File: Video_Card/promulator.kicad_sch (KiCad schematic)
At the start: 16 parts, among them J2 Conn_01x06_Pin, J3 Conn_01x05_Socket, U5 PIC18F15Q40, U7 EPF81188AQC208-3

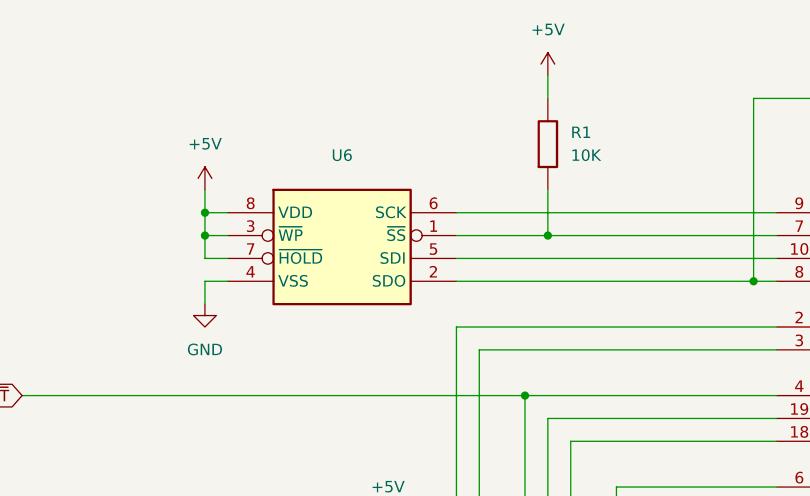
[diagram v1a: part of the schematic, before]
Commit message: Todays work:
* Added clock identifier to SPI flash clock input
* Add config pins to FPGA host interface - can be used for configuring address decoding
* Add FPGA clocks sheet
* Add expansion ROM sheet
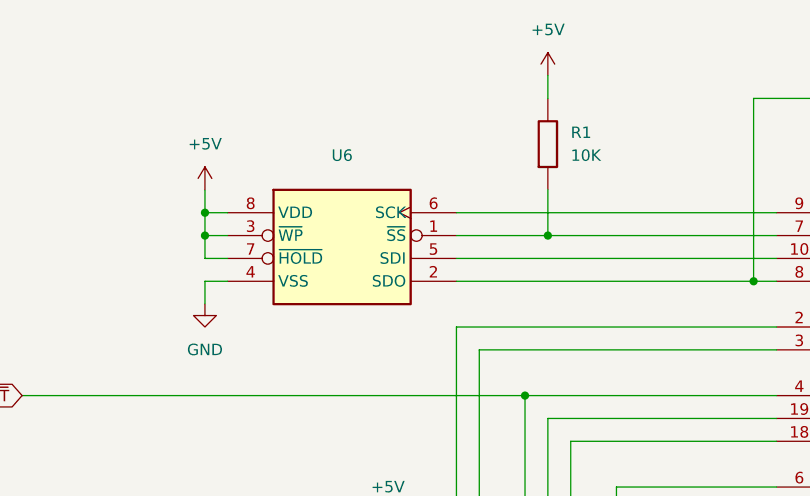
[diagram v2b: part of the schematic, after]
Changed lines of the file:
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@@
 	)
 	(symbol
-		(lib_name "Video_Card:FPGA_dev")
 		(lib_id "Video_Card:FPGA_dev")
 		(at 48.26 175.26 0)
@@
 		)
 		(pin "154"
+		)
+		(pin ""
+		)
+		(pin ""
+		)
+		(pin ""
+		)
+		(pin ""
+		)
+		(pin ""
+		)
+		(pin ""
+		)
+		(pin ""
+		)
+		(pin ""
+		)
+		(pin ""
+		)
+		(pin ""
+		)
+		(pin ""
+		)
+		(pin ""
+		)
+		(pin ""
+		)
+		(pin ""
+		)
+		(pin ""
+		)
+		(pin ""
 		)
 		(pin ""
@@
 	)
 	(symbol
+		(lib_name "Video_Card:FPGA_dev")
 		(lib_id "Video_Card:FPGA_dev")
 		(at 215.9 50.8 0)
@@
 		)
 		(pin ""
+		)
+		(pin ""
+		)
+		(pin ""
+		)
+		(pin ""
+		)
+		(pin ""
+		)
+		(pin ""
+		)
+		(pin ""
+		)
+		(pin ""
+		)
+		(pin ""
+		)
+		(pin ""
+		)
+		(pin ""
+		)
+		(pin ""
+		)
+		(pin ""
+		)
+		(pin ""
+		)
+		(pin ""
+		)
+		(pin ""
+		)
+		(pin ""

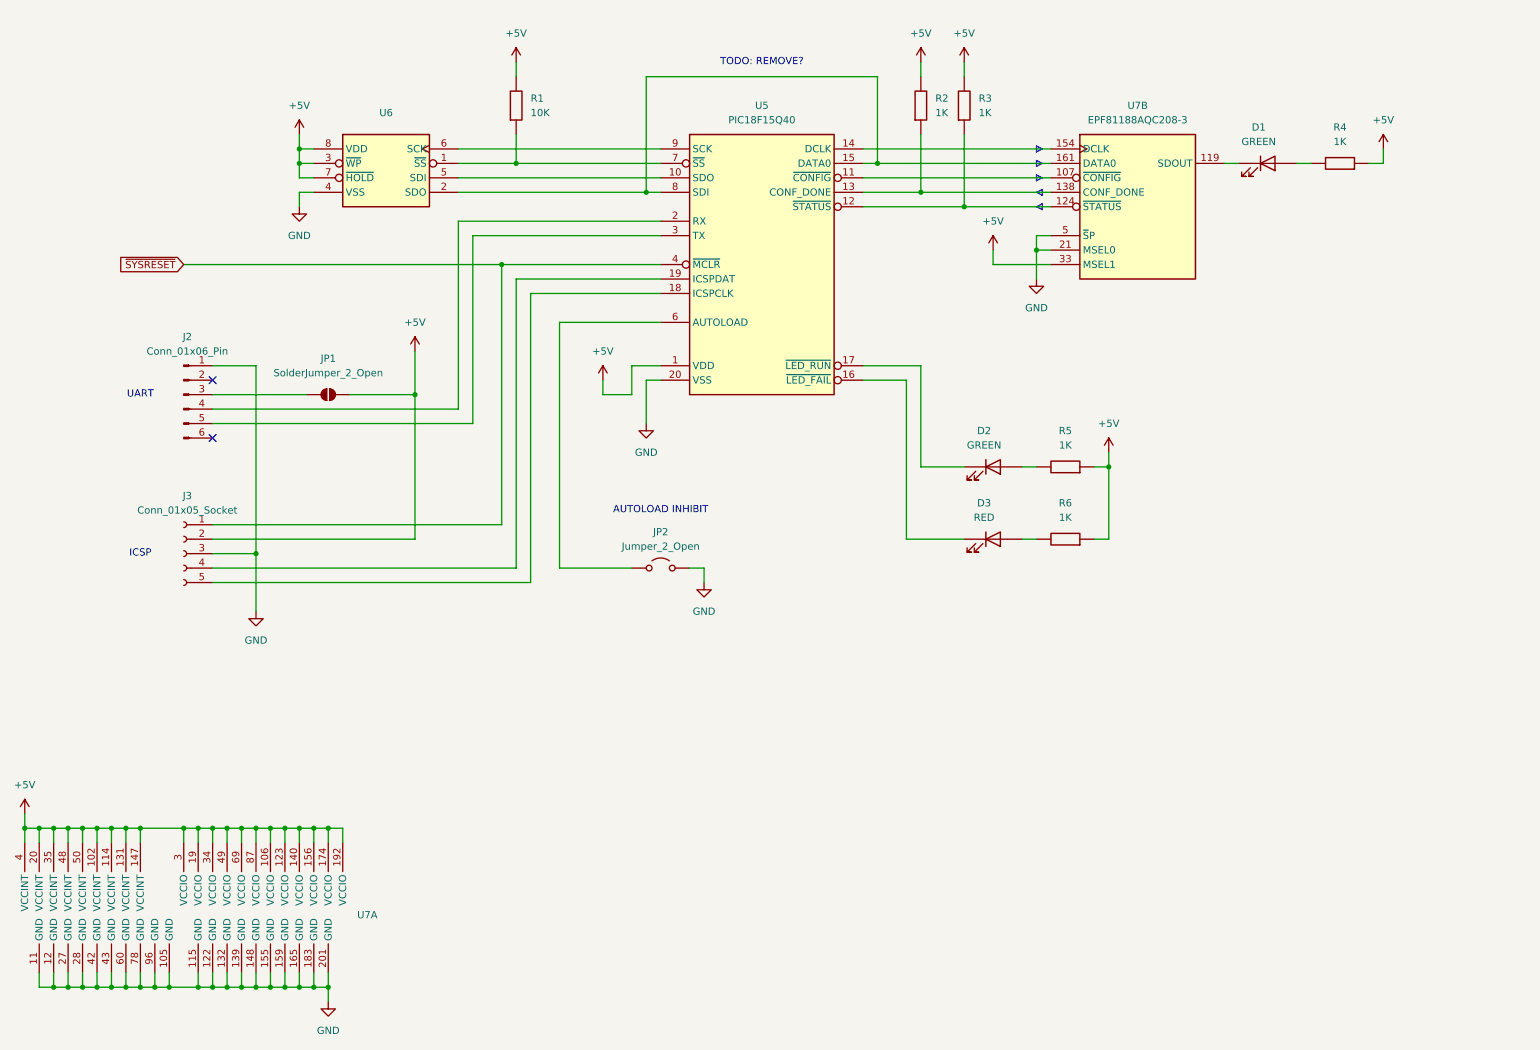
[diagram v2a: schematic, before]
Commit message: Work to date:
* added RAMDAC sheet
* tweaks to promulator circuit to disconnect MCLR, and add future reset output
* tweaks to FPGA host interface, add pin numbers and rearrange reset input to allow reset either from the system or from the promulator following configuration
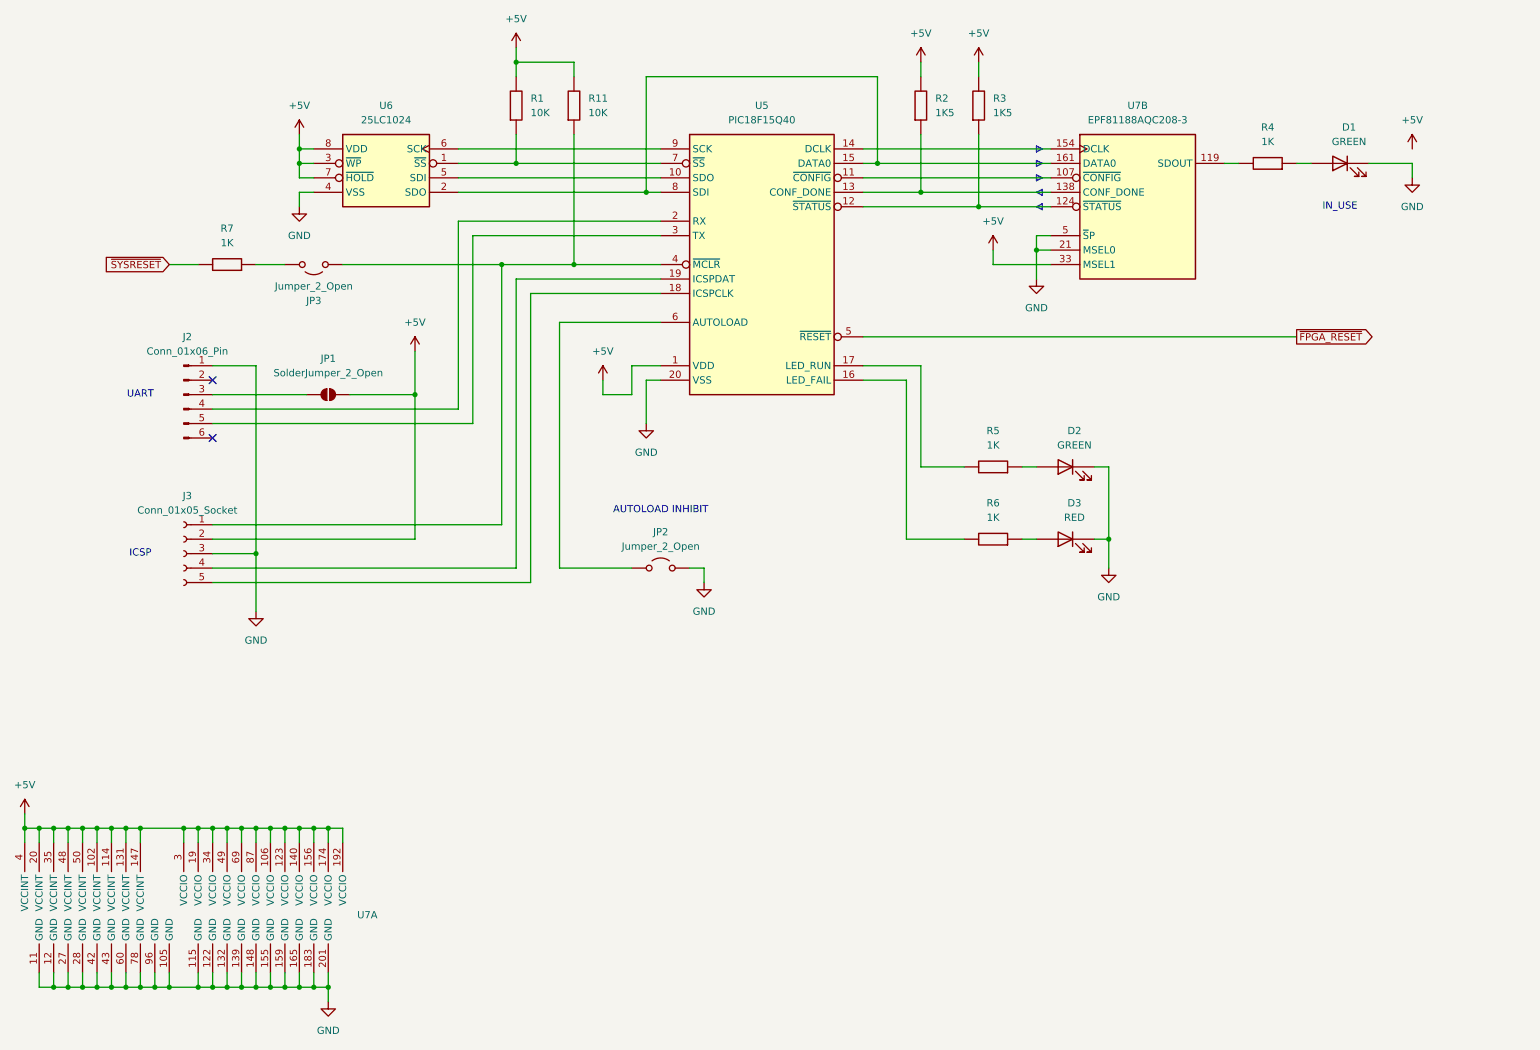
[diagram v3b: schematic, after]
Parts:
- added JP3: Jumper_2_Open, Connector_PinHeader_2.54mm:PinHeader_1x02_P2.54mm_Vertical, symbol Jumper:Jumper_2_Open
- added R11: 10K, COMET_footprints:R_SMD0805, symbol COMET_symbols:R
- added R7: 1K, COMET_footprints:R_SMD0805, symbol COMET_symbols:R
- R2, R3: value 1K -> 1K5
- U6: value ~ -> 25LC1024
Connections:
- net +5V: now also R11.1; no longer R4.2, R5.2, R6.2
- net GND: now also D1.1 (K), D2.1 (K), D3.1 (K)
- net ~{SYSRESET}: now also R7.1; no longer J3.1 (Pin_1), U5.4 (~{MCLR})
- net at R5.1: now also U5.17 (LED_RUN); no longer D2.2 (A)
- net at R6.1: now also U5.16 (LED_FAIL); no longer D3.2 (A)
- net at U7.119 (SDOUT): now also R4.1; no longer D1.1 (K)
- net at D1.2 (A): now also R4.2; no longer R4.1
- new net: J3.1 (Pin_1), JP3.2 (B), R11.2, U5.4 (~{MCLR})
- new net: D2.2 (A), R5.2
- new net: JP3.1 (A), R7.2
- new net: D3.2 (A), R6.2
- new net ~{FPGA_RESET}: U5.5 (~{RESET})
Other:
- note added: "IN_USE"
- note removed: "TODO: REMOVE?"
- moved on the sheet: R3

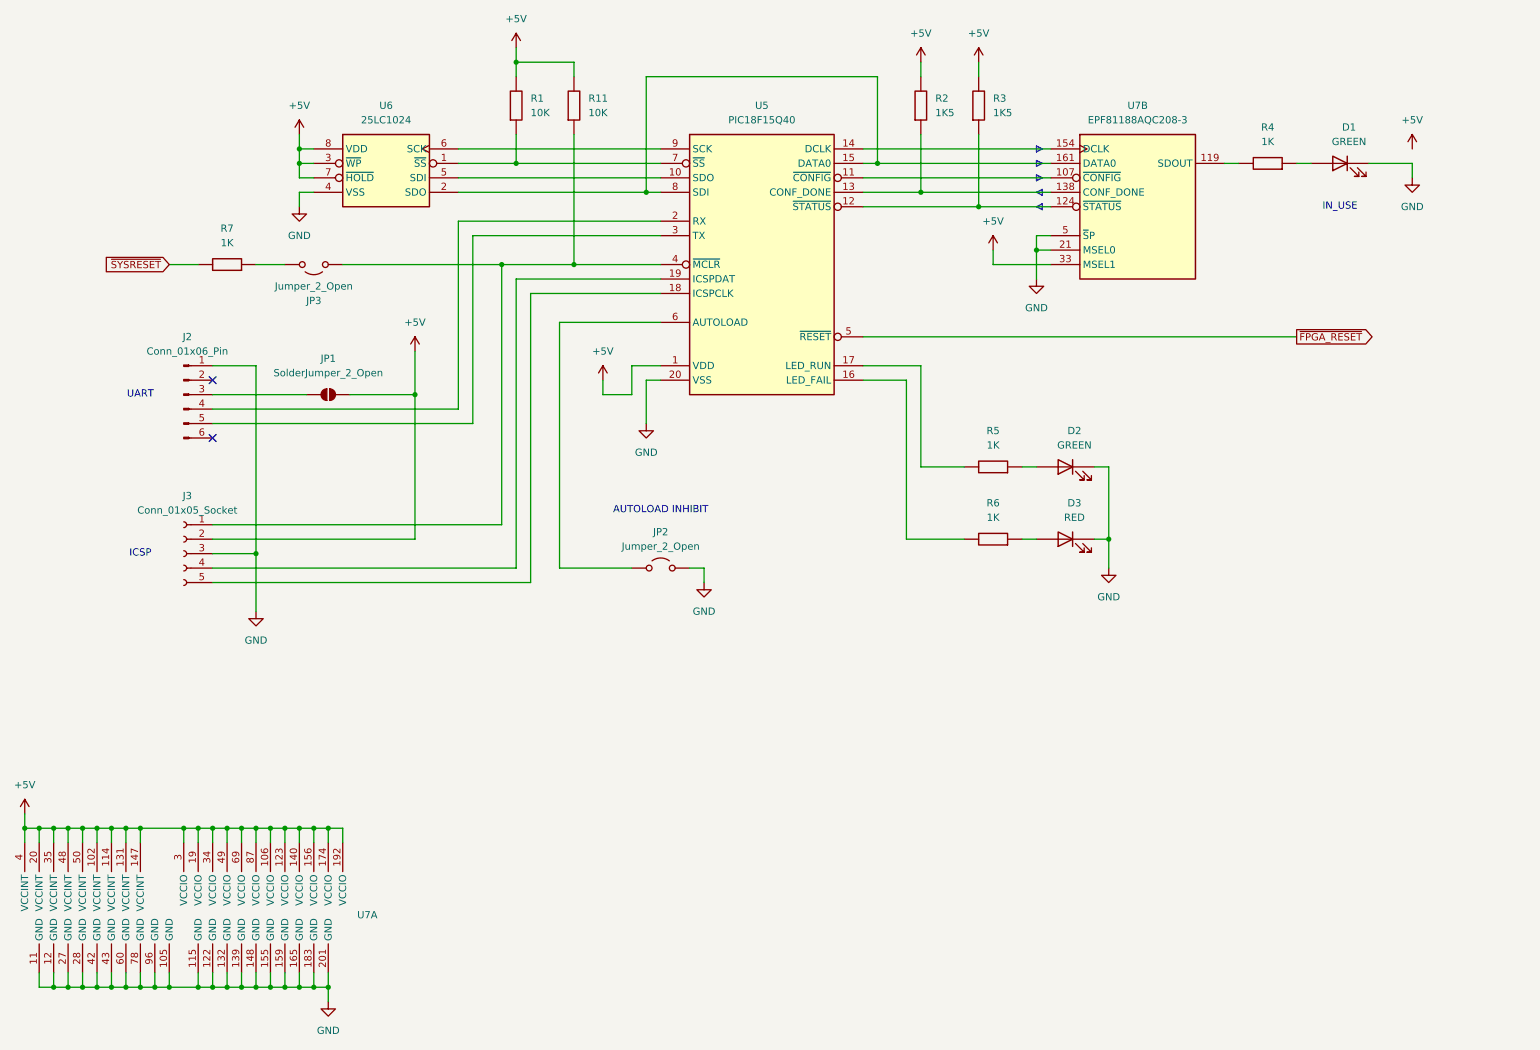
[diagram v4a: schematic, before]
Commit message: Work to date
So much to list ....

* Changed expansion ROM to 16 bit wide to remove some components
* Tried moving peripherals over to an 8 bit dedicated bus, but will have to revert this to reduce component count
* Fleshed out keyboard and I2C controller circuits
* Tried to fit in a font RAM, but I am 50/50 whether this will stick

And a lot more I am sure.
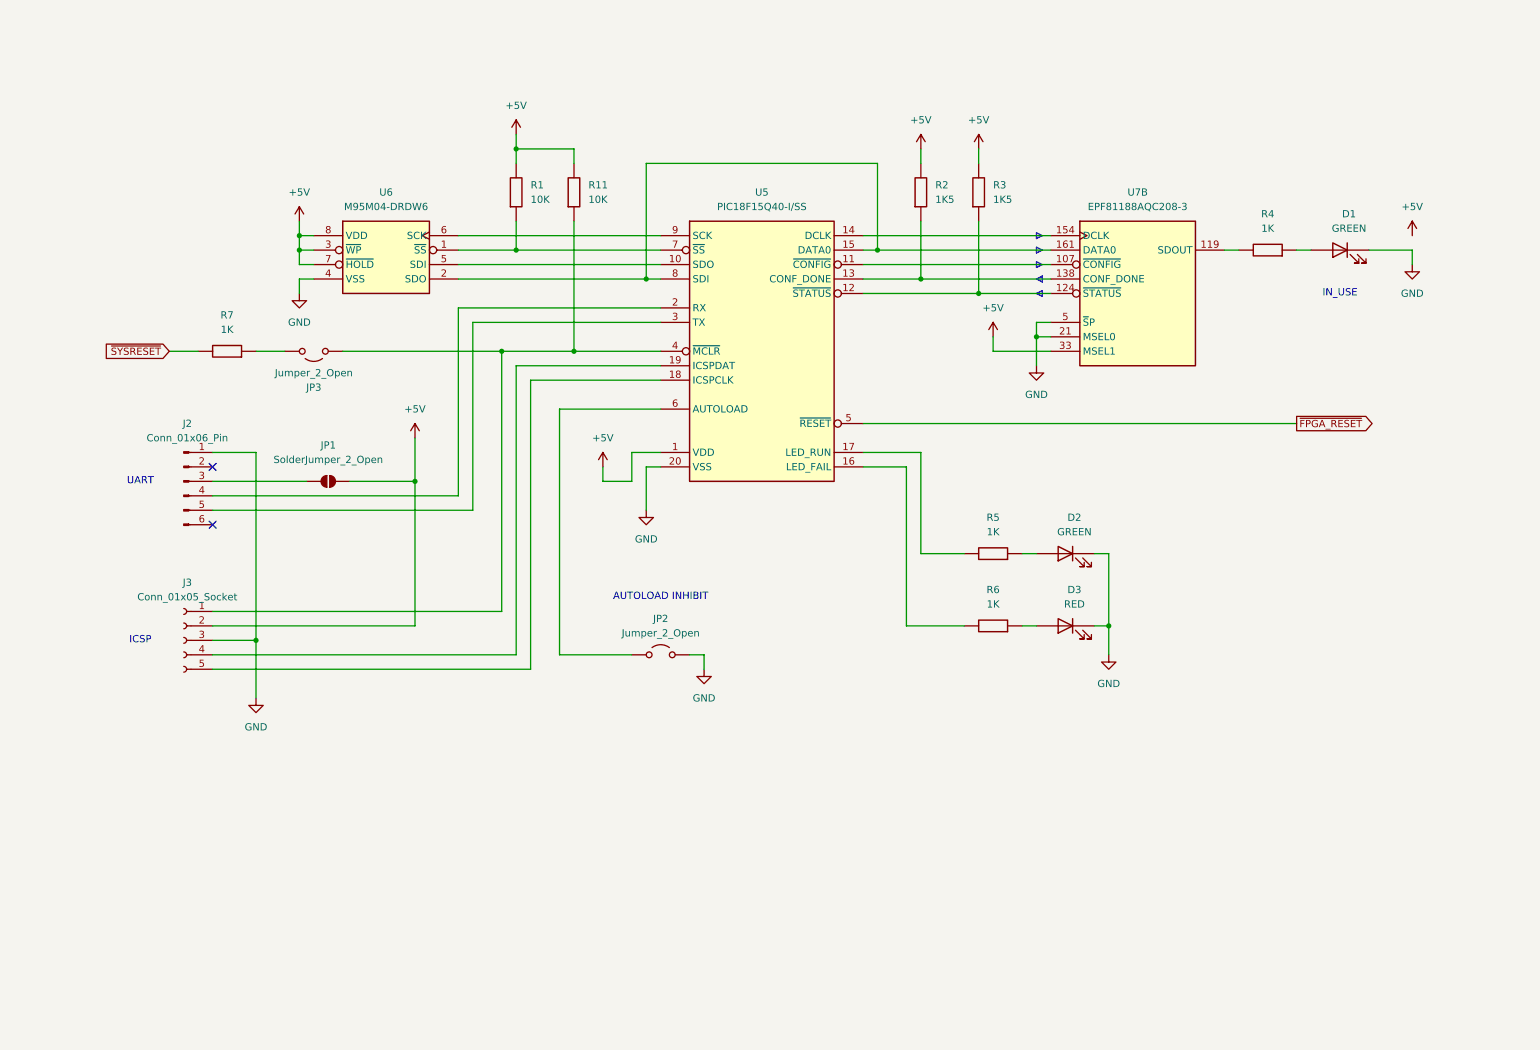
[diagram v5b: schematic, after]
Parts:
- removed unit 1 of U7
- U5: value PIC18F15Q40 -> PIC18F15Q40-I/SS; footprint COMET_footprints:Package_SO20W -> Video_Card:Package_SSOP-20_5.3x7.2mm_P0.65_MCHP
- U6: value 25LC1024 -> M95M04-DRDW6; footprint COMET_footprints:Package_TSSOP-8_3x3mm_P0.65mm -> COMET_footprints:Package_TSSOP-8_4.4x3mm_P0.65mm
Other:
- moved on the sheet: D1, D2, D3, J2, J3, JP1, JP2, JP3, R1, R11, R2, R3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

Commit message: Final work for rev 1
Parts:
- JP2: renamed from JP1; footprint Jumper:SolderJumper-2_P1.3mm_Open_RoundedPad1.0x1.5mm -> Jumper:SolderJumper-2_P1.3mm_Open_TrianglePad1.0x1.5mm
- U5: renamed from U7; symbol Video_Card:FPGA_dev -> Video_Card:EPF81188AQC208-3
- renumbered JP3 to JP1, JP2 to JP3, R11 to R2, R2 to R3, R3 to R4, R4 to R5, R7 to R6, R5 to R7, R6 to R8, U6 to U26, U5 to U27
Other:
- note added: "ACTIVE SERIAL RESERVED PASSIVE SERIAL ** RESERVED ACTIVE PARALLEL UP PASSIVE PARALLEL SYNC ACTIVE PARALLEL DOWN PASSIVE PARALLEL ASYNC"
- note added: "MODE AS RESERVED PS RESERVED APU PPS APD PPA"
- note added: "MSEL0 0 1 0 1 0 1 0 1"
- note added: "MSEL1 0 0 1 1 0 0 1 1"
- note added: "~{S}P 0 0 0 0 1 1 1 1"
